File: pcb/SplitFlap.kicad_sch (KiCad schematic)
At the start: 20 parts, among them U1 PCF8575DBR, U2 ULN2003, U4 AP2112K-3.3

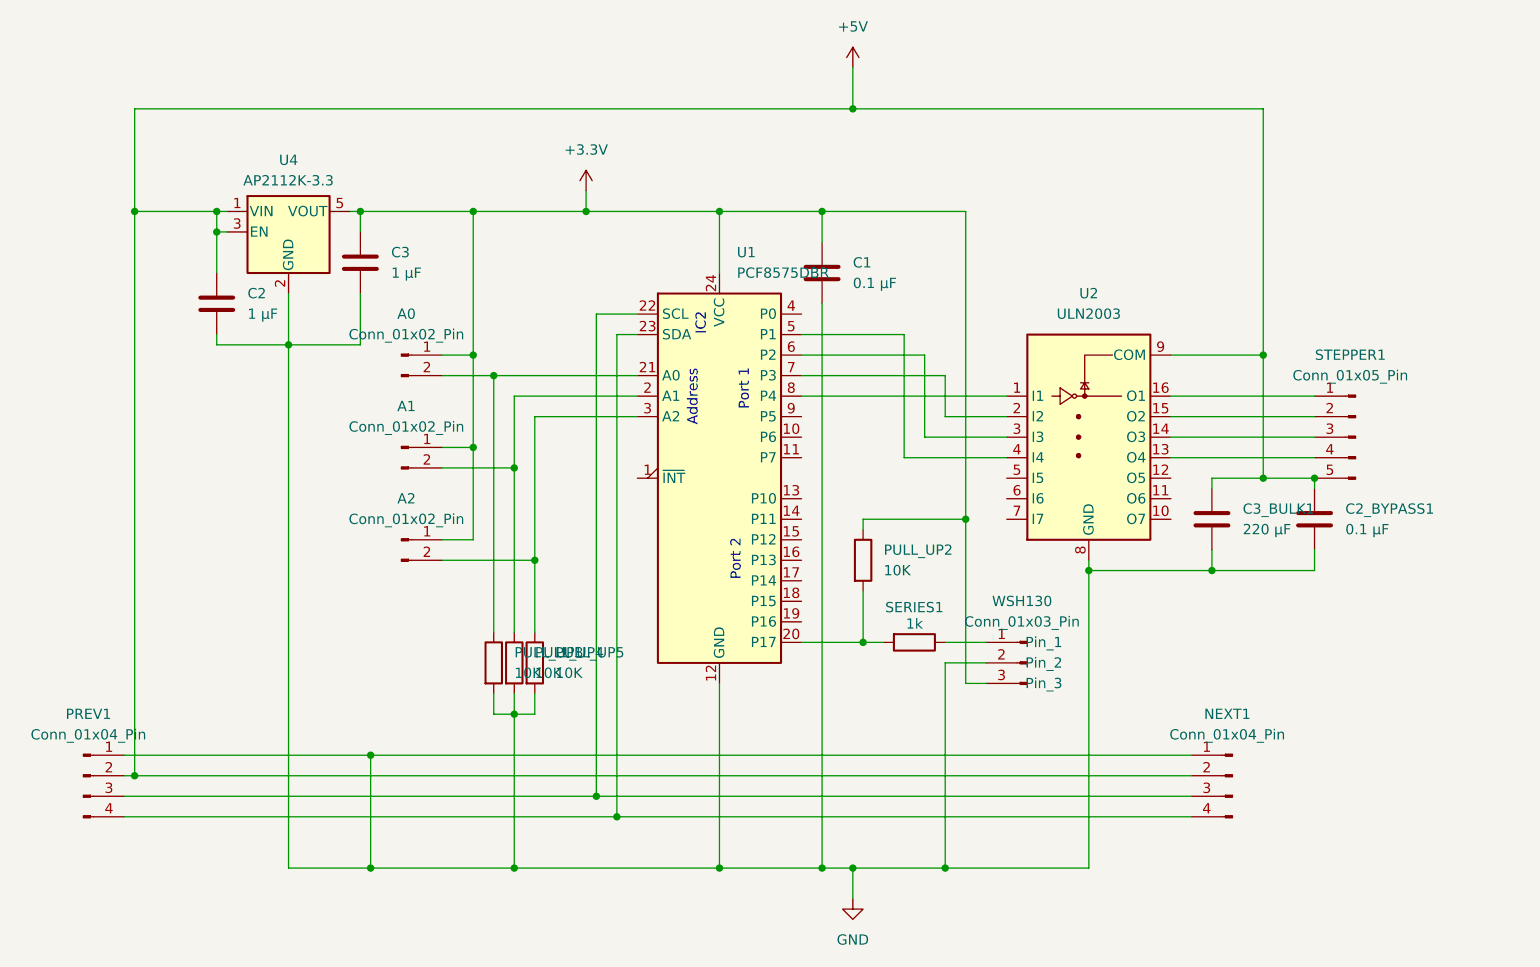
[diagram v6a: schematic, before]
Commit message: Add pull-ups between PCF8575 and ULN2003
This is necessary since the PCF8575 can only pull the output to 0, not
bring it up to 3.3v, so a pull-up is necessary to communicate with the
ULN2003 (which only responds to values 2.5v or above).
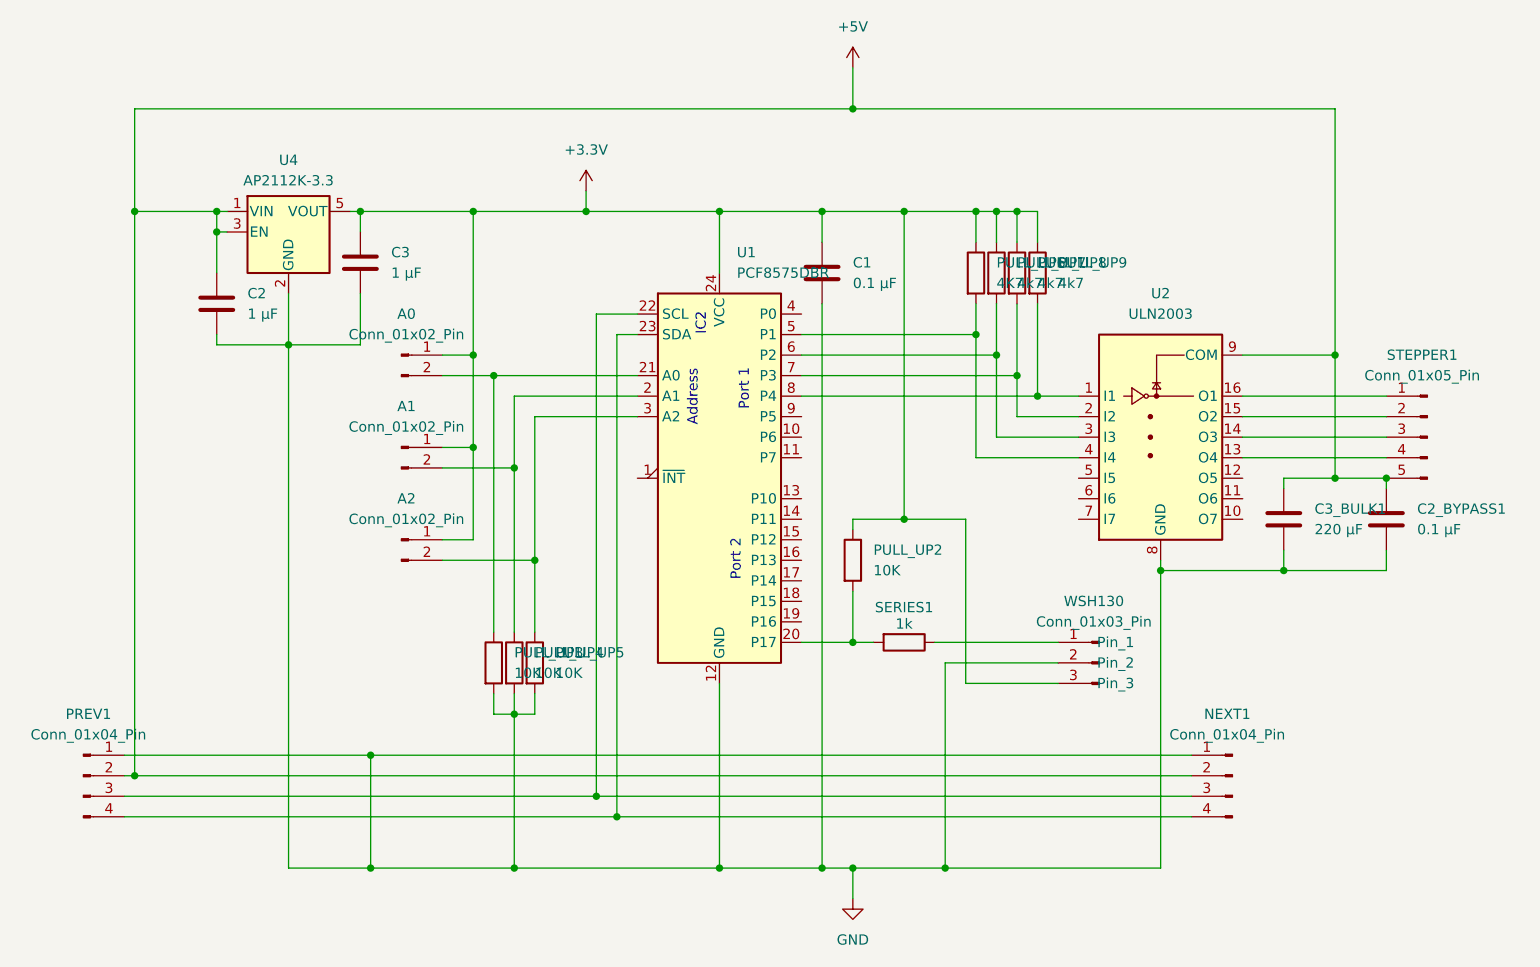
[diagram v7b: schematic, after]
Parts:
- added PULL_UP6: 4K7, Resistor_SMD:R_0603_1608Metric, symbol Device:R
- added PULL_UP7, PULL_UP8, PULL_UP9: 4k7, Resistor_SMD:R_0603_1608Metric, symbol Device:R
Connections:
- net +3.3V: now also PULL_UP6.1, PULL_UP7.1, PULL_UP8.1, PULL_UP9.1
- net at U1.8 (P4), U2.1 (I1): now also PULL_UP9.2
- net at U1.7 (P3), U2.2 (I2): now also PULL_UP8.2
- net at U1.6 (P2), U2.3 (I3): now also PULL_UP7.2
- net at U1.5 (P1), U2.4 (I4): now also PULL_UP6.2
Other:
- moved on the sheet: C2_BYPASS1, C3_BULK1, PULL_UP2, SERIES1, STEPPER1, U2, WSH130

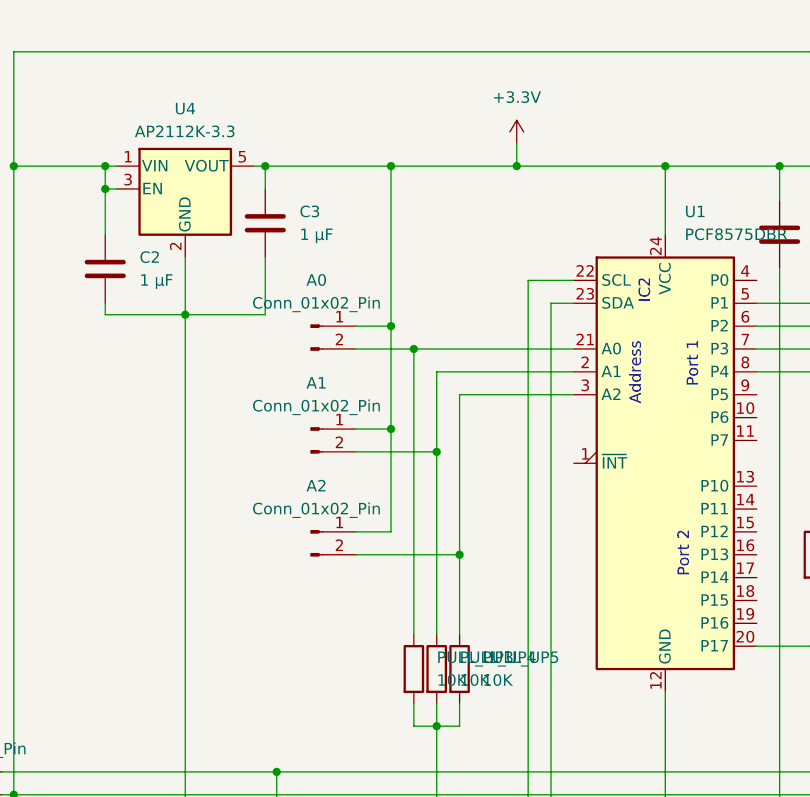
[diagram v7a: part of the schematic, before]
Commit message: Use 2x3 connector for address pins
Saves on board space and component count
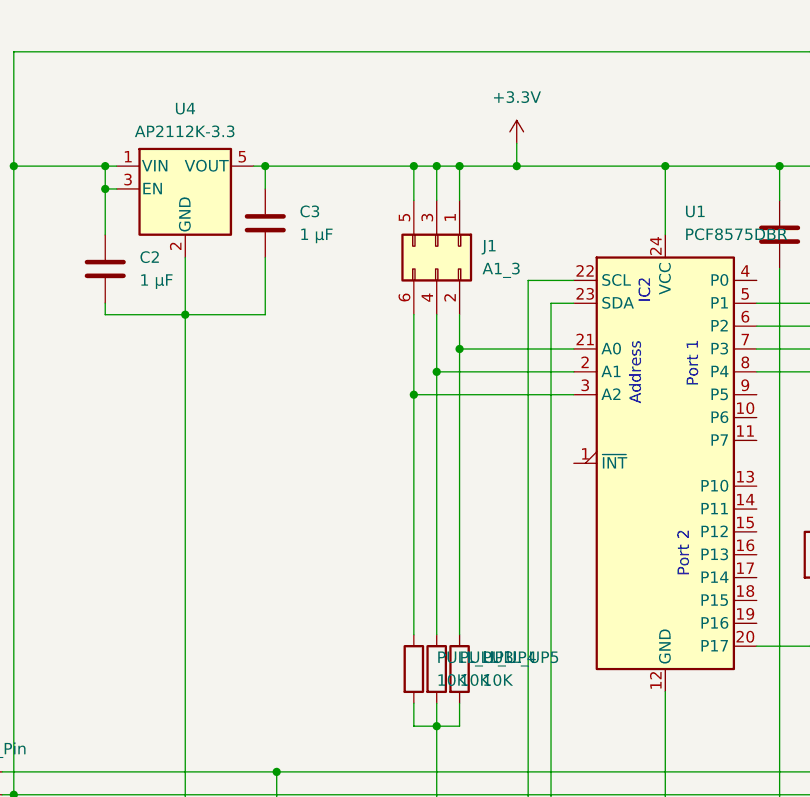
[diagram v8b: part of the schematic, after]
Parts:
- removed A0, A1, A2: Conn_01x02_Pin, Connector_PinHeader_2.54mm:PinHeader_1x02_P2.54mm_Vertical, symbol Connector:Conn_01x02_Pin
- added J1: A1_3, Connector_PinHeader_2.54mm:PinHeader_2x03_P2.54mm_Vertical, symbol Connector_Generic:Conn_02x03_Odd_Even
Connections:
- net +3.3V: now also J1.1 (Pin_1), J1.3 (Pin_3), J1.5 (Pin_5)
- net at U1.3 (A2): now also PULL_UP3.1, J1.6 (Pin_6); no longer PULL_UP5.1
- net at U1.21 (A0): now also PULL_UP5.1, J1.2 (Pin_2); no longer PULL_UP3.1
- net at PULL_UP4.1, U1.2 (A1): now also J1.4 (Pin_4)
